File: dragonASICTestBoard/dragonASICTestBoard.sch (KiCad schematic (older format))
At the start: 5 parts, among them P1 CONN_01X20, P2 CONN_01X20, P3 CONN_01X20, P4 CONN_01X20, U1 die80

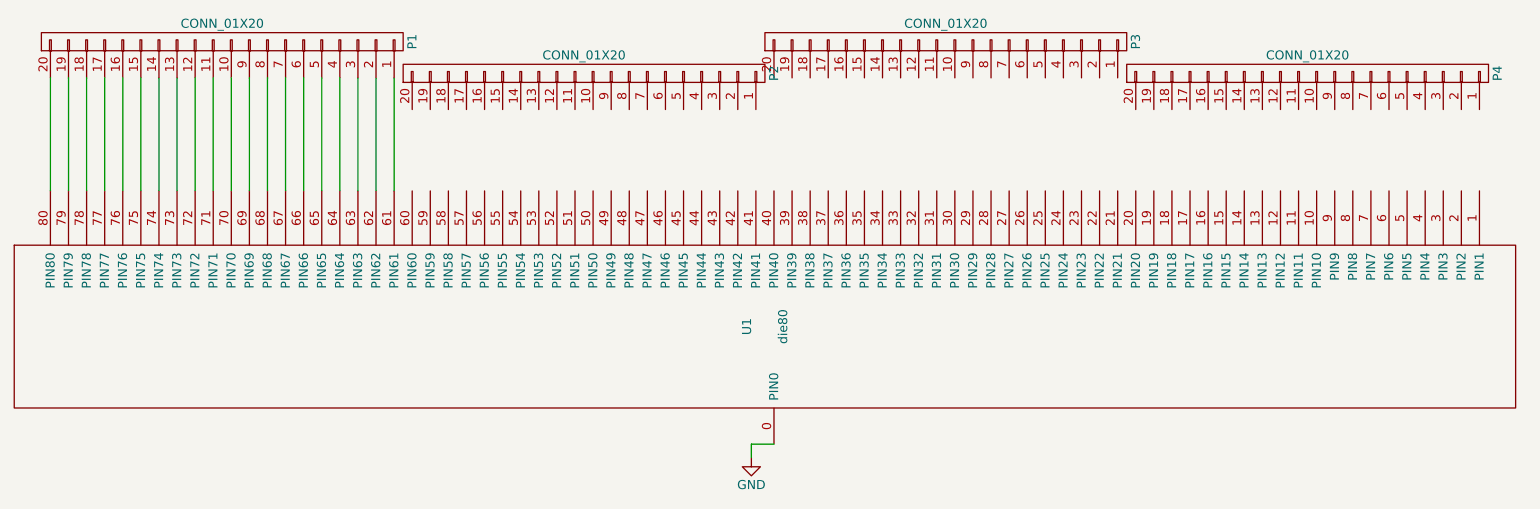
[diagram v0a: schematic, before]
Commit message: Add PCB layout to dragonASICTestBoard
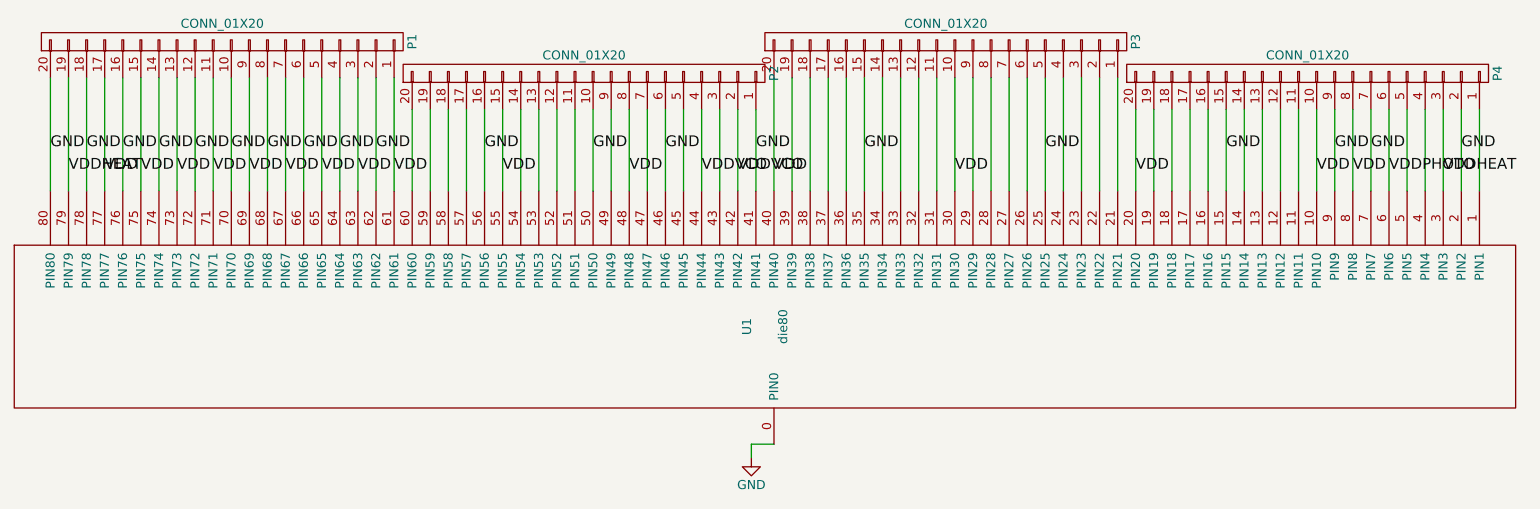
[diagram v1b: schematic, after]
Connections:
- net GND: now also P1.10 (P10), P1.12 (P12), P1.14 (P14), P1.16 (P16), P1.18 (P18), P1.2 (P2), P1.20 (P20), P1.4 (P4), P1.6 (P6), P1.8 (P8), P2.1 (P1), P2.10 (P10), P2.16 (P16), P2.6 (P6), P3.15 (P15), P3.5 (P5), P4.15 (P15), P4.2 (P2), P4.7 (P7), P4.9 (P9), U1.15 (PIN15), U1.2 (PIN2), U1.25 (PIN25), U1.35 (PIN35), U1.41 (PIN41), U1.46 (PIN46), U1.50 (PIN50), U1.56 (PIN56), U1.62 (PIN62), U1.64 (PIN64), U1.66 (PIN66), U1.68 (PIN68), U1.7 (PIN7), U1.70 (PIN70), U1.72 (PIN72), U1.74 (PIN74), U1.76 (PIN76), U1.78 (PIN78), U1.80 (PIN80), U1.9 (PIN9)
- net at U1.1 (PIN1): now also P4.1 (P1)
- net VDD: now reaches U1.10 (PIN10)
- net VDD: now also P1.1 (P1), P1.11 (P11), P1.13 (P13), P1.15 (P15), P1.17 (P17), P1.3 (P3), P1.5 (P5), P1.7 (P7), P1.9 (P9), P2.15 (P15), P2.8 (P8), P3.10 (P10), P3.20 (P20), P4.10 (P10), P4.20 (P20), P4.8 (P8), U1.20 (PIN20), U1.30 (PIN30), U1.40 (PIN40), U1.48 (PIN48), U1.55 (PIN55), U1.61 (PIN61), U1.63 (PIN63), U1.65 (PIN65), U1.67 (PIN67), U1.69 (PIN69), U1.71 (PIN71), U1.73 (PIN73), U1.75 (PIN75), U1.77 (PIN77), U1.8 (PIN8)
- net at U1.11 (PIN11): now also P4.11 (P11)
- net at U1.12 (PIN12): now also P4.12 (P12)
- net at U1.13 (PIN13): now also P4.13 (P13)
- net at U1.14 (PIN14): now also P4.14 (P14)
- net at U1.16 (PIN16): now also P4.16 (P16)
- net at U1.17 (PIN17): now also P4.17 (P17)
- net at U1.18 (PIN18): now also P4.18 (P18)
- net at U1.19 (PIN19): now also P4.19 (P19)
- net at U1.21 (PIN21): now also P3.1 (P1)
- net at U1.22 (PIN22): now also P3.2 (P2)
- net at U1.23 (PIN23): now also P3.3 (P3)
- net at U1.24 (PIN24): now also P3.4 (P4)
- net at U1.26 (PIN26): now also P3.6 (P6)
- net at U1.27 (PIN27): now also P3.7 (P7)
- net at U1.28 (PIN28): now also P3.8 (P8)
- net at U1.29 (PIN29): now also P3.9 (P9)
- net VDDHEAT: now reaches U1.3 (PIN3)
- net VDDHEAT: now also P1.19 (P19), P4.3 (P3), U1.79 (PIN79)
- net at U1.31 (PIN31): now also P3.11 (P11)
- net at U1.32 (PIN32): now also P3.12 (P12)
- net at U1.33 (PIN33): now also P3.13 (P13)
- net at U1.34 (PIN34): now also P3.14 (P14)
- net at U1.36 (PIN36): now also P3.16 (P16)
- net at U1.37 (PIN37): now also P3.17 (P17)
- net at U1.38 (PIN38): now also P3.18 (P18)
- net at U1.39 (PIN39): now also P3.19 (P19)
- net at U1.4 (PIN4): now also P4.4 (P4)
- net VDDVCO: now reaches U1.42 (PIN42)
- net VDDVCO: now also P2.2 (P2), P2.4 (P4), U1.44 (PIN44)
- net at U1.43 (PIN43): now also P2.3 (P3)
- net at U1.45 (PIN45): now also P2.5 (P5)
- net at U1.47 (PIN47): now also P2.7 (P7)
- net at U1.49 (PIN49): now also P2.9 (P9)
- net at U1.5 (PIN5): now also P4.5 (P5)
- net at U1.51 (PIN51): now also P2.11 (P11)
- net at U1.52 (PIN52): now also P2.12 (P12)
- net at U1.53 (PIN53): now also P2.13 (P13)
- net at U1.54 (PIN54): now also P2.14 (P14)
- net at U1.57 (PIN57): now also P2.17 (P17)
- net at U1.58 (PIN58): now also P2.18 (P18)
- net at U1.59 (PIN59): now also P2.19 (P19)
- net VDDPHOTO: now reaches U1.6 (PIN6)
- net VDDPHOTO: now also P4.6 (P6)
- net at U1.60 (PIN60): now also P2.20 (P20)
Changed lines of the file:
@@
 LIBS:valves
 LIBS:dragonASICTestBoard
+LIBS:dragonASICTestBoard-cache
 EELAYER 25 0
 EELAYER END
@@
 	1    0    0    -1
 $EndComp
-Wire Wire Line
-	6375 4675 6250 4675
-Wire Wire Line
-	6250 4675 6250 4750
 $Comp
 L CONN_01X20 P4
@@
 $EndComp
 Wire Wire Line
+	6375 4675 6250 4675
+Wire Wire Line
+	6250 4675 6250 4750
+Wire Wire Line
 	2375 2650 2375 3275
 Wire Wire Line
@@
 Wire Wire Line
 	4275 3275 4275 2650
+Wire Wire Line
+	4375 2825 4375 3275
+Wire Wire Line
+	4475 2825 4475 3275
+Wire Wire Line
+	4575 2825 4575 3275
+Wire Wire Line
+	4675 3275 4675 2825
+Wire Wire Line
+	4775 2825 4775 3275
+Wire Wire Line
+	4875 3275 4875 2825
+Wire Wire Line
+	4975 2825 4975 3275
+Wire Wire Line
+	5075 3275 5075 2825
+Wire Wire Line
+	5175 2825 5175 3275
+Wire Wire Line
+	5275 3275 5275 2825
+Wire Wire Line
+	5375 2825 5375 3275
+Wire Wire Line
+	5475 2825 5475 3275
+Wire Wire Line
+	5575 2825 5575 3275
+Wire Wire Line
+	5675 2825 5675 3275
+Wire Wire Line
+	5775 2825 5775 3275
+Wire Wire Line
+	5875 3275 5875 2825
+Wire Wire Line
+	5975 2825 5975 3275
+Wire Wire Line
+	6075 3275 6075 2825
+Wire Wire Line
+	6175 2825 6175 3275
+Wire Wire Line
+	6275 3275 6275 2825
+Wire Wire Line
+	6375 2650 6375 3275
+Wire Wire Line
+	6475 3275 6475 2650
+Wire Wire Line
+	6575 2650 6575 3275
+Wire Wire Line
+	6675 3275 6675 2650
+Wire Wire Line
+	6775 2650 6775 3275
+Wire Wire Line
+	6875 2650 6875 3275
+Wire Wire Line
+	6975 3275 6975 2650
+Wire Wire Line
+	7075 2650 7075 3275
+Wire Wire Line
+	7175 3275 7175 2650
+Wire Wire Line
+	7275 2650 7275 3275
+Wire Wire Line
+	7375 3275 7375 2650
+Wire Wire Line
+	7475 2650 7475 3275
+Wire Wire Line
+	7575 3275 7575 2650
+Wire Wire Line
+	7675 2650 7675 3275
+Wire Wire Line
+	7775 3275 7775 2650
+Wire Wire Line
+	7875 2650 7875 3275
+Wire Wire Line
+	7975 3275 7975 2650
+Wire Wire Line
+	8075 2650 8075 3275
+Wire Wire Line
+	8175 3275 8175 2650
+Wire Wire Line
+	8275 2650 8275 3275
+Wire Wire Line
+	8375 3275 8375 2825
+Wire Wire Line
+	8475 2825 8475 3275
+Wire Wire Line
+	8575 3275 8575 2825
+Wire Wire Line
+	8675 2825 8675 3275
+Wire Wire Line
+	8775 3275 8775 2825
+Wire Wire Line
+	8875 2825 8875 3275
+Wire Wire Line
+	8975 3275 8975 2825
+Wire Wire Line
+	9075 2825 9075 3275
+Wire Wire Line
+	9175 3275 9175 2825
+Wire Wire Line
+	9275 2825 9275 3275
+Wire Wire Line
+	9375 3275 9375 2825
+Wire Wire Line
+	9475 2825 9475 3275
+Wire Wire Line
+	9575 3275 9575 2825
+Wire Wire Line
+	9675 2825 9675 3275
+Wire Wire Line
+	9775 3275 9775 2825
+Wire Wire Line
+	9875 2825 9875 3275
+Wire Wire Line
+	9975 3275 9975 2825
+Wire Wire Line
+	10075 2825 10075 3275
+Wire Wire Line
+	10175 2825 10175 3275
+Wire Wire Line
+	10275 3275 10275 2825
+Text Label 10175 3050 0    60   ~ 0
+GND
+Text Label 9675 3050 0    60   ~ 0
+GND
+Text Label 9475 3050 0    60   ~ 0
+GND
+Text Label 8875 3050 0    60   ~ 0
+GND
+Text Label 7875 3050 0    60   ~ 0
+GND
+Text Label 6875 3050 0    60   ~ 0
+GND
+Text Label 6275 3050 0    60   ~ 0
+GND
+Text Label 5775 3050 0    60   ~ 0
+GND
+Text Label 5375 3050 0    60   ~ 0
+GND
+Text Label 4775 3050 0    60   ~ 0
+GND
+Text Label 4175 3050 0    60   ~ 0
+GND
+Text Label 3975 3050 0    60   ~ 0
+GND
+Text Label 3775 3050 0    60   ~ 0
+GND
+Text Label 3575 3050 0    60   ~ 0
+GND
+Text Label 3375 3050 0    60   ~ 0
+GND
+Text Label 3175 3050 0    60   ~ 0
+GND
+Text Label 2975 3050 0    60   ~ 0
+GND
+Text Label 2775 3050 0    60   ~ 0
+GND
+Text Label 2575 3050 0    60   ~ 0
+GND
+Text Label 2375 3050 0    60   ~ 0
+GND
+Text Label 10075 3175 0    60   ~ 0
+VDDHEAT
+Text Label 9775 3175 0    60   ~ 0
+VDDPHOTO
+Text Label 9575 3175 0    60   ~ 0
+VDD
+Text Label 9375 3175 0    60   ~ 0
+VDD
+Text Label 8375 3175 0    60   ~ 0
+VDD
+Text Label 7375 3175 0    60   ~ 0
+VDD
+Text Label 6375 3175 0    60   ~ 0
+VDD
+Text Label 6175 3175 0    60   ~ 0
+VDDVCO
+Text Label 5975 3175 0    60   ~ 0
+VDDVCO
+Text Label 5575 3175 0    60   ~ 0
+VDD
+Text Label 4875 3175 0    60   ~ 0
+VDD
+Text Label 4275 3175 0    60   ~ 0
+VDD
+Text Label 4075 3175 0    60   ~ 0
+VDD
+Text Label 3875 3175 0    60   ~ 0
+VDD
+Text Label 3675 3175 0    60   ~ 0
+VDD
+Text Label 3475 3175 0    60   ~ 0
+VDD
+Text Label 3275 3175 0    60   ~ 0
+VDD
+Text Label 3075 3175 0    60   ~ 0
+VDD
+Text Label 2875 3175 0    60   ~ 0
+VDD
+Text Label 2675 3175 0    60   ~ 0
+VDD
+Text Label 2475 3175 0    60   ~ 0
+VDDHEAT
 $EndSCHEMATC
